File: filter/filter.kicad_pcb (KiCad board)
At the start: 2 copper layers, 10 parts, among them J101 TRX, J102 TRX

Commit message: filter backup
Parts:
- J101, J102, L101, L102: moved to B.Cu
- moved C104 47.8 mm to (143.5, 85.1), turned to 270 degrees
- moved C101 37.5 mm to (153.0, 91.4), turned to 180 degrees
- moved C105 28.0 mm to (160.0, 87.6), turned to 270 degrees
- moved C106 25.0 mm to (160.0, 82.5), turned to 90 degrees
- moved C103 22.2 mm to (153.0, 88.9), turned to 180 degrees
- moved C102 17.6 mm to (157.5, 82.5), turned to 90 degrees
- moved J102 16.4 mm to (166.4, 81.3), turned to 180 degrees
- moved J101 14.1 mm to (139.7, 81.3), turned to 180 degrees
- moved L101 8.76 mm to (147.3, 77.5), turned to 270 degrees
- moved L102 7.30 mm to (158.8, 92.5), turned to 90 degrees
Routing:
- net Net-(C101-Pad1): track 0.00 -> 19.1 mm
- net Net-(C102-Pad2): track 0.00 -> 13.6 mm
- net Net-(C104-Pad1): track 0.00 -> 12.5 mm
- net Net-(C101-Pad2): track 0.00 -> 7.64 mm
- added copper zone on B.Cu, net GND
- added copper zone on F.Cu, net GND
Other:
- board outline added: 31.8 x 20.3 mm
- board text added: "m"

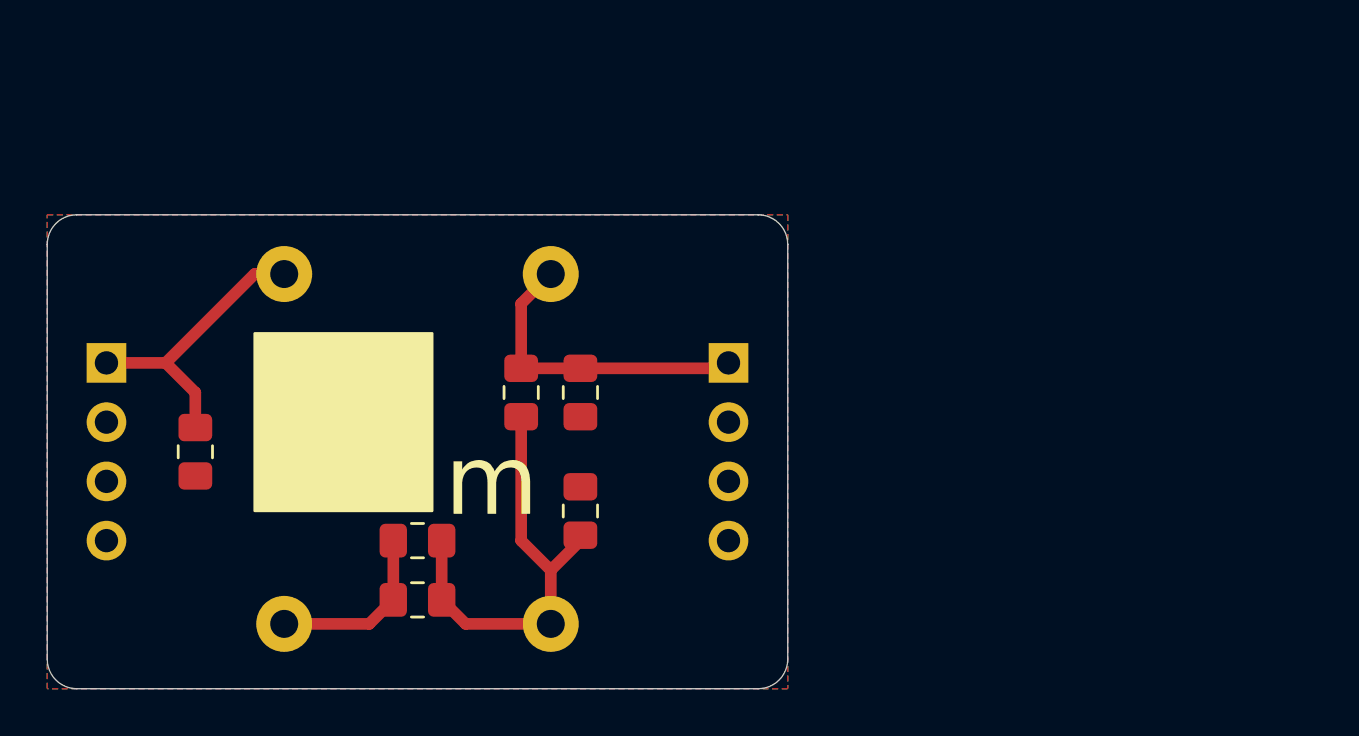
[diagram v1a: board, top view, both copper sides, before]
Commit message: Filter updated
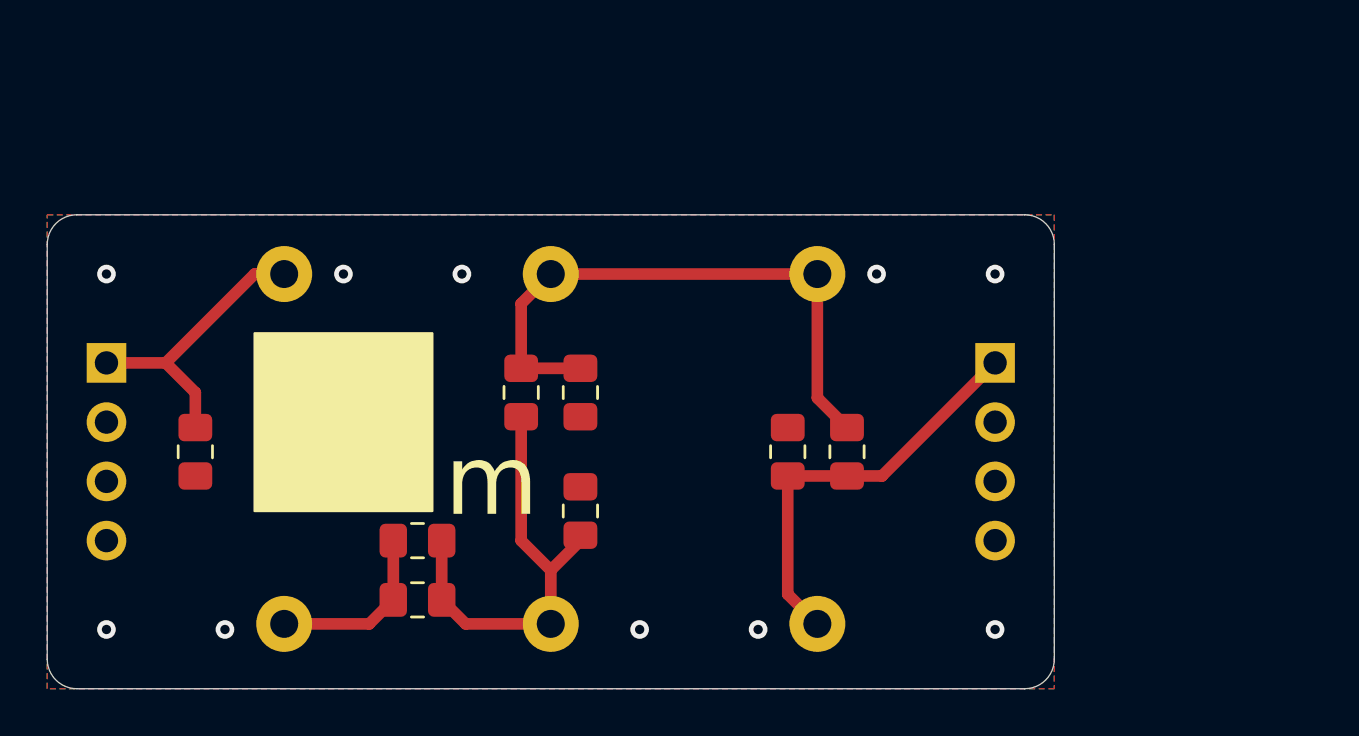
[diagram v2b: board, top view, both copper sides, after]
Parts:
- added C1: 0, Capacitor_SMD:C_0805_2012Metric_Pad1.18x1.45mm_HandSolder, F.Cu at (171.4, 85.1)
- added C2: 0, Capacitor_SMD:C_0805_2012Metric_Pad1.18x1.45mm_HandSolder, F.Cu at (168.9, 85.1)
- added L1: 0, Inductor_THT:L_Toroid_Horizontal_D9.5mm_P15.00mm_Diameter10-5mm_Amidon-T37, B.Cu at (170.2, 77.5)
- C101: value C -> 1p
- C102: value C -> 330p
- C103: value C -> 1000p
- C104: value C -> 360p
- C105: value C -> 620p
- C106: value C -> 470p
- L101: value T37 -> 675n
- L102: value T37 -> 243n
- moved J102 11.4 mm to (177.8, 81.3)
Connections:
- C102 pad 2: Net-(C102-Pad2) -> Net-(C1-Pad1)
- C106 pad 2: Net-(C102-Pad2) -> Net-(C1-Pad1)
- J101 pad 2: Net-(J101-Pad2) -> GND
- J101 pad 3: Net-(J101-Pad3) -> GND
- J102 pad 1: Net-(C102-Pad2) -> Net-(C1-Pad2)
- J102 pad 2: Net-(J102-Pad2) -> GND
- J102 pad 3: Net-(J102-Pad3) -> GND
- L102 pad 2: Net-(C102-Pad2) -> Net-(C1-Pad1)
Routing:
- net Net-(C1-Pad1): track 0.00 -> 25.6 mm
- net Net-(C1-Pad2): track 0.00 -> 17.8 mm
- net Net-(C102-Pad2): track 13.6 -> 0.00 mm
- net GND: vias 0 -> 10
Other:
- board size 31.8 x 20.3 mm -> 43.2 x 20.3 mm
